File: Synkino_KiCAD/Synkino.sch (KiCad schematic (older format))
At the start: 88 parts

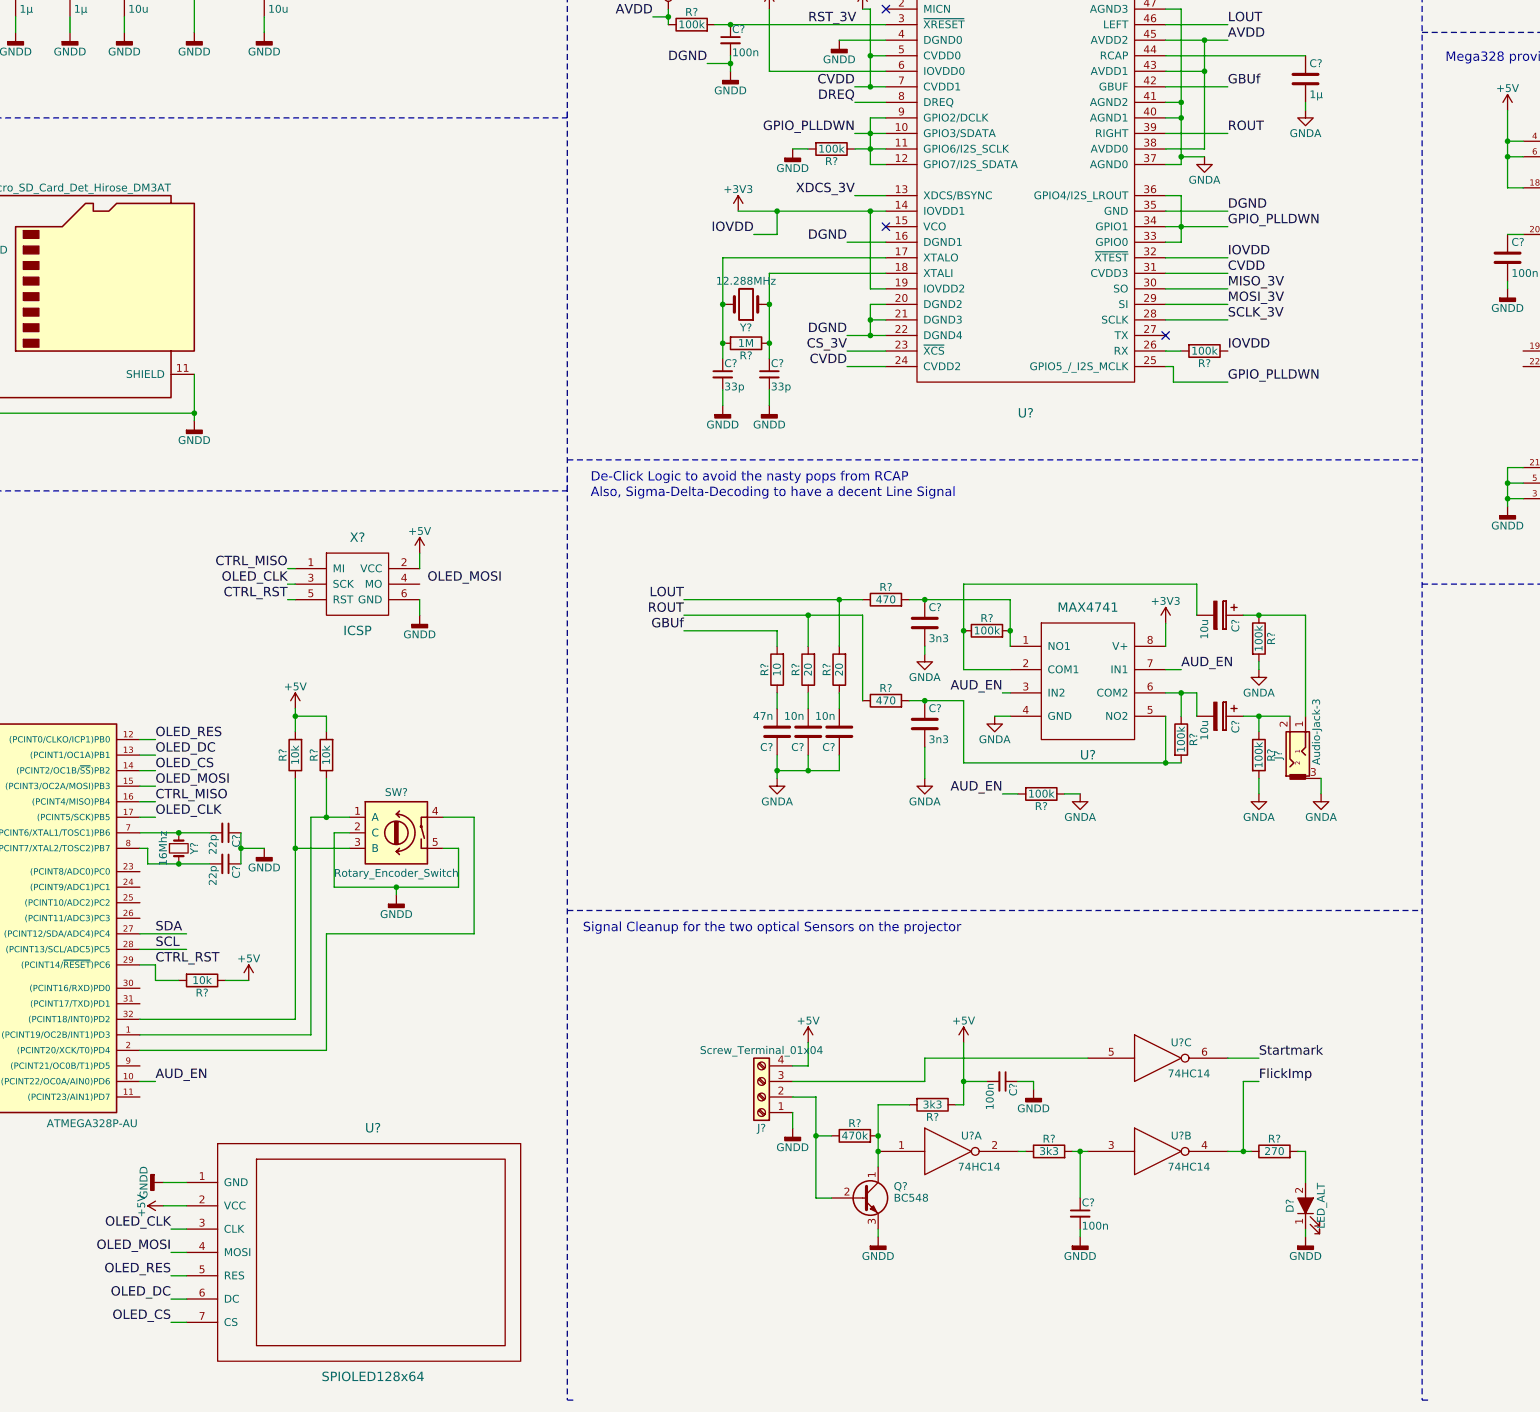
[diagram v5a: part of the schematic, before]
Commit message: Adding ICSP to both uCs
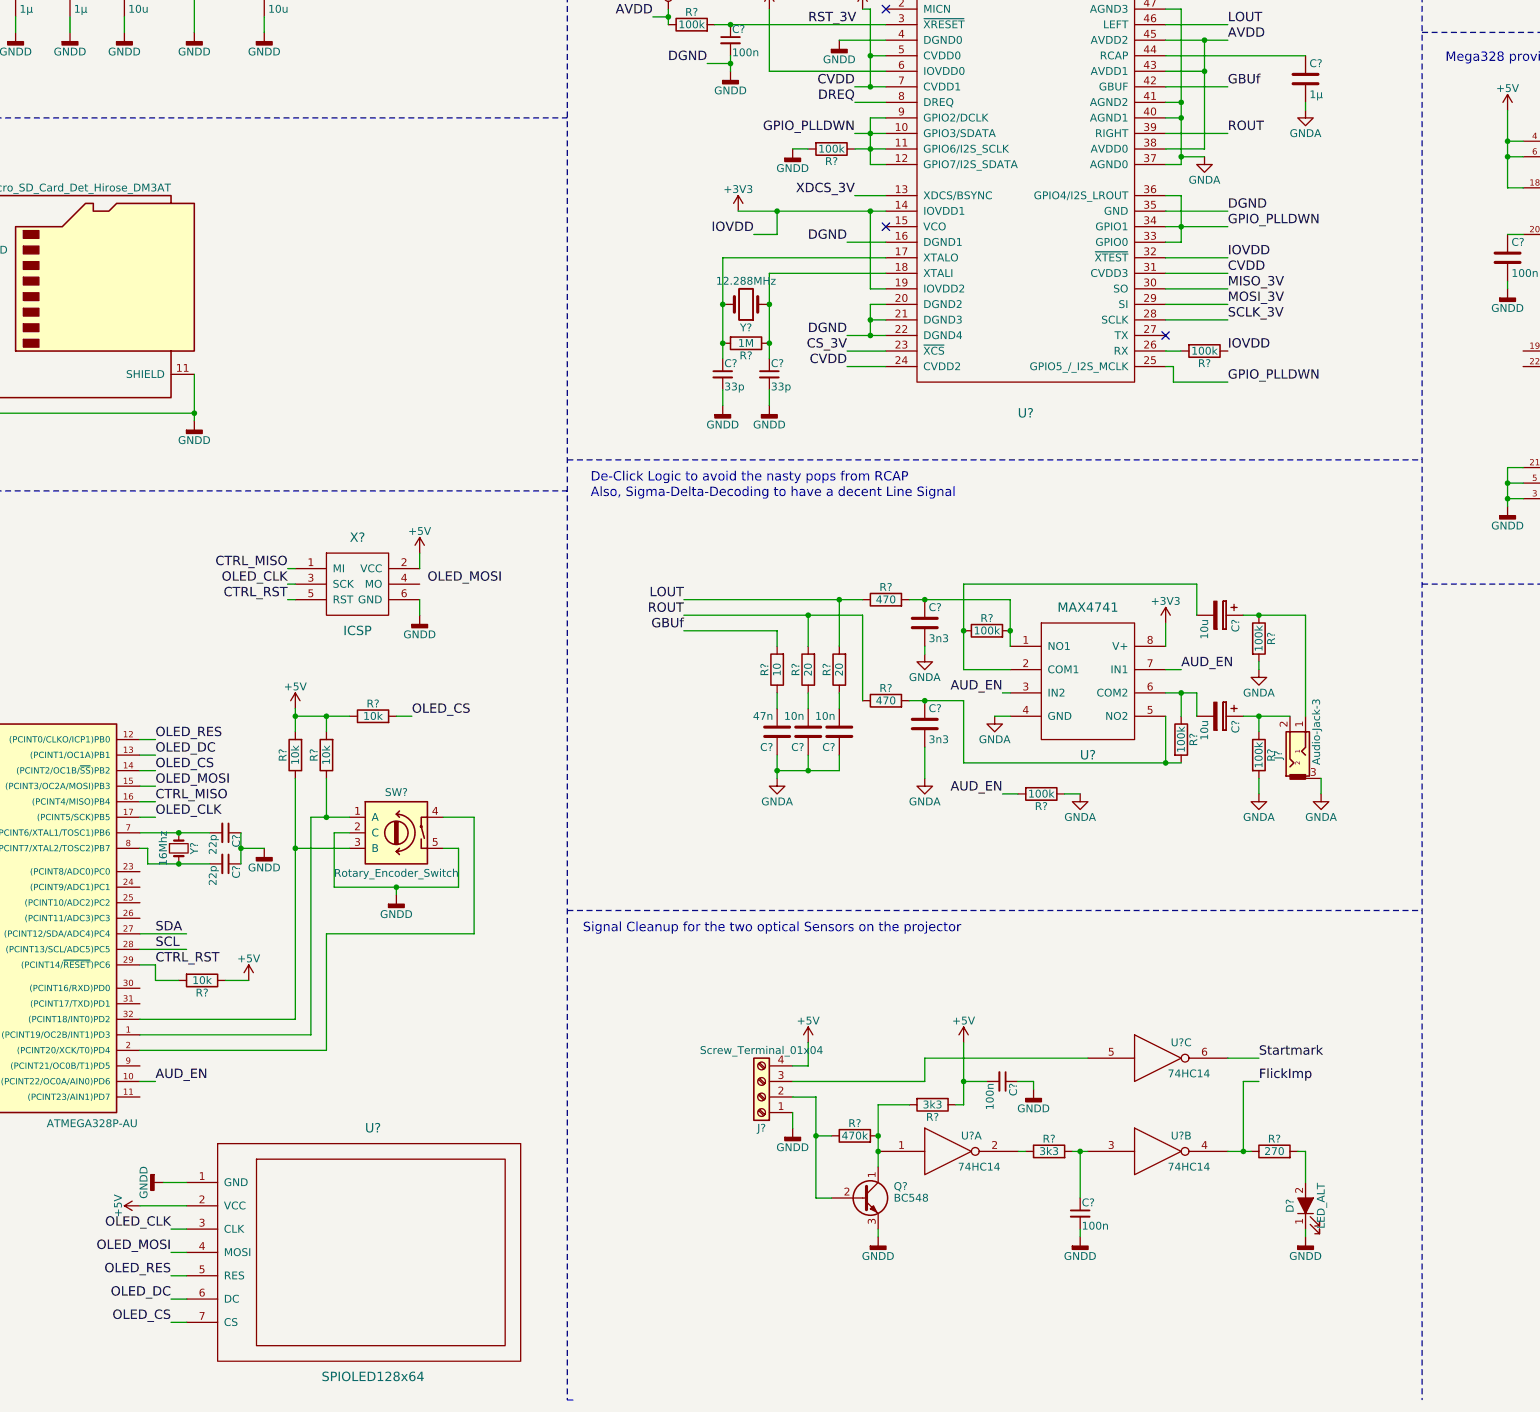
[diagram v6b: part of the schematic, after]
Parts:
- added R?: 10k, symbol R
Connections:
- net +5V: now also R?.1
- net OLED_CS: now also R?.2
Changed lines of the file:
@@
 L +5V #PWR?
 U 1 1 5A9C29C5
-P 3000 9950
-F 0 "#PWR?" H 3000 9800 50  0001 C CNN
-F 1 "+5V" H 3000 10090 50  0000 C CNN
-F 2 "" H 3000 9950 50  0001 C CNN
-F 3 "" H 3000 9950 50  0001 C CNN
-	1    3000 9950
+P 2850 9950
+F 0 "#PWR?" H 2850 9800 50  0001 C CNN
+F 1 "+5V" H 2850 10090 50  0000 C CNN
+F 2 "" H 2850 9950 50  0001 C CNN
+F 3 "" H 2850 9950 50  0001 C CNN
+	1    2850 9950
 	0    -1   -1   0
 $EndComp
@@
 	3000 9800 3150 9800
 Wire Wire Line
-	3000 9950 3150 9950
+	2850 9950 3150 9950
 Text Label 2950 7450 0    60   ~ 0
 OLED_CLK
@@
 	4050 6900 4050 6800
 Wire Wire Line
-	4050 6800 3850 6800
+	3850 6800 4200 6800
 Connection ~ 3850 6800
 Wire Wire Line
@@
 	5000 7450 4800 7450
 Wire Notes Line
-	5600 500  5600 11200
-Wire Notes Line
 	5600 11200 5650 11200
 Wire Notes Line
 	11100 500  11100 11200
 Wire Notes Line
-	11100 11200 11150 11200
-Wire Notes Line
 	500  2950 5600 2950
 Wire Notes Line
-	5600 2950 5600 2900
-Wire Notes Line
 	500  5350 5600 5350
-Wire Notes Line
-	5600 5350 5600 5250
 Wire Notes Line
 	5600 5150 11100 5150
@@
 Wire Wire Line
 	2900 7650 2900 7750
+Wire Notes Line
+	5600 500  5600 11200
+$Comp
+L R R?
+U 1 1 5A9CE1EA
+P 4350 6800
+F 0 "R?" V 4430 6800 50  0000 C CNN
+F 1 "10k" V 4350 6800 50  0000 C CNN
+F 2 "" V 4280 6800 50  0001 C CNN
+F 3 "" H 4350 6800 50  0001 C CNN
+	1    4350 6800
+	0    -1   -1   0
+$EndComp
+Connection ~ 4050 6800
+Text Label 4600 6800 0    60   ~ 0
+OLED_CS
+Wire Wire Line
+	4500 6800 4600 6800
 $EndSCHEMATC

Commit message: Adding FTDI Jumpers
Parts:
- added C? (x2): 100n, symbol C_Small
- added X? (x2): FTDIconn, symbol FTDIconn
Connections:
- net +5V: now also X?.3 (VCC), X?.3 (VCC)
- net CTRL_RST: now also C?.1
- net GNDD: now also X?.1 (GND), X?.1 (GND), X?.2 (CTS), X?.2 (CTS)
- net ~RST: now also C?.1
- net AU_RXD: now reaches U?.30 ((PCINT16/RXD)PD0)
- net AU_RXD: now also X?.4 (TXO)
- net AU_TXD: now reaches U?.31 ((PCINT17/TXD)PD1)
- net AU_TXD: now also X?.5 (RXI)
- net CTRL_RXD: now reaches U?.30 ((PCINT16/RXD)PD0)
- net CTRL_RXD: now also X?.4 (TXO)
- net CTRL_TXD: now reaches U?.31 ((PCINT17/TXD)PD1)
- net CTRL_TXD: now also X?.5 (RXI)
- new net: C?.2, X?.6 (DTR) (x2)
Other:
- moved on the sheet: R?
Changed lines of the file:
@@
 LIBS:spioled128x64
 LIBS:icsp
+LIBS:ftdi
 LIBS:Synkino-cache
 EELAYER 25 0
@@
 $EndComp
 Wire Wire Line
-	11750 5200 11650 5200
+	11550 5200 11750 5200
 Wire Wire Line
 	11650 5200 11650 5450
@@
 Text Label 13750 4450 0    60   ~ 0
 SCL
-Wire Wire Line
-	13650 4350 13950 4350
-Wire Wire Line
-	13650 4450 13950 4450
 $Comp
 L R R?
 U 1 1 5A9D1C9B
+P 14100 4150
+F 0 "R?" V 14180 4150 50  0000 C CNN
+F 1 "10k" V 14100 4150 50  0000 C CNN
+F 2 "" V 14030 4150 50  0001 C CNN
+F 3 "" H 14100 4150 50  0001 C CNN
+	1    14100 4150
+	0    1    1    0
+$EndComp
+$Comp
+L R R?
+U 1 1 5A9D1E44
 P 14100 4350
 F 0 "R?" V 14180 4350 50  0000 C CNN
@@
 	0    1    1    0
 $EndComp
-$Comp
-L R R?
-U 1 1 5A9D1E44
-P 14100 4450
-F 0 "R?" V 14180 4450 50  0000 C CNN
-F 1 "10k" V 14100 4450 50  0000 C CNN
-F 2 "" V 14030 4450 50  0001 C CNN
-F 3 "" H 14100 4450 50  0001 C CNN
-	1    14100 4450
-	0    1    1    0
-$EndComp
-Wire Wire Line
-	14250 4350 14300 4350
-Wire Wire Line
-	14300 4350 14300 4550
+Wire Wire Line
+	14300 4150 14300 4550
 Connection ~ 14300 4550
-Wire Wire Line
-	14250 4450 14300 4450
-Connection ~ 14300 4450
 $Comp
 L ATMEGA328P-AU U?
@@
 L R R?
 U 1 1 5A9D65E3
-P 3250 8500
-F 0 "R?" V 3330 8500 50  0000 C CNN
-F 1 "10k" V 3250 8500 50  0000 C CNN
-F 2 "" V 3180 8500 50  0001 C CNN
-F 3 "" H 3250 8500 50  0001 C CNN
-	1    3250 8500
+P 3600 8400
+F 0 "R?" V 3680 8400 50  0000 C CNN
+F 1 "10k" V 3600 8400 50  0000 C CNN
+F 2 "" V 3530 8400 50  0001 C CNN
+F 3 "" H 3600 8400 50  0001 C CNN
+	1    3600 8400
 	0    1    1    0
 $EndComp
@@
 L +5V #PWR?
 U 1 1 5A9D65E9
-P 3550 8500
-F 0 "#PWR?" H 3550 8350 50  0001 C CNN
-F 1 "+5V" H 3550 8640 50  0000 C CNN
-F 2 "" H 3550 8500 50  0001 C CNN
-F 3 "" H 3550 8500 50  0001 C CNN
-	1    3550 8500
+P 3750 8250
+F 0 "#PWR?" H 3750 8100 50  0001 C CNN
+F 1 "+5V" H 3750 8390 50  0000 C CNN
+F 2 "" H 3750 8250 50  0001 C CNN
+F 3 "" H 3750 8250 50  0001 C CNN
+	1    3750 8250
 	1    0    0    -1
 $EndComp
@@
 CTRL_RST
 Wire Wire Line
-	2850 8400 2950 8400
+	2850 8400 3450 8400
 Text Label 3800 6050 2    60   ~ 0
 CTRL_RST
@@
 Wire Wire Line
 	3800 6050 3850 6050
-Wire Wire Line
-	2950 8400 2950 8500
-Wire Wire Line
-	2950 8500 3100 8500
-Wire Wire Line
-	3400 8500 3550 8500
 Wire Wire Line
 	2850 7650 2900 7650
@@
 Wire Wire Line
 	4500 6800 4600 6800
+$Comp
+L FTDIconn X?
+U 1 1 5A9C7C58
+P 15000 4350
+F 0 "X?" H 15000 4800 60  0000 C CNN
+F 1 "FTDIconn" H 15000 3900 60  0000 C CNN
+F 2 "" H 15000 4400 60  0001 C CNN
+F 3 "" H 15000 4400 60  0001 C CNN
+	1    15000 4350
+	1    0    0    -1
+$EndComp
+Text Label 11550 5200 2    60   ~ 0
+GNDD
+Connection ~ 11650 5200
+Text Label 15400 4100 0    60   ~ 0
+GNDD
+Text Label 15400 4200 0    60   ~ 0
+GNDD
+Text Label 11550 2950 2    60   ~ 0
+5V
+Wire Wire Line
+	11550 2950 11650 2950
+Connection ~ 11650 2950
+Text Label 15400 4300 0    60   ~ 0
+5V
+Wire Wire Line
+	15300 4100 15400 4100
+Wire Wire Line
+	15300 4200 15400 4200
+Wire Wire Line
+	15300 4300 15400 4300
+Text Label 13750 4700 0    60   ~ 0
+AU_RXD
+Text Label 13750 4800 0    60   ~ 0
+AU_TXD
+Wire Wire Line
+	13650 4700 13750 4700
+Wire Wire Line
+	13650 4800 13750 4800
+Text Label 15400 4400 0    60   ~ 0
+AU_RXD
+Text Label 15400 4500 0    60   ~ 0
+AU_TXD
+Wire Wire Line
+	15300 4400 15400 4400
+Wire Wire Line
+	15300 4500 15400 4500
+$Comp
+L C_Small C?
+U 1 1 5A9C9C74
+P 15500 4600
+F 0 "C?" H 15510 4670 50  0000 L CNN
+F 1 "100n" H 15510 4520 50  0000 L CNN
+F 2 "" H 15500 4600 50  0001 C CNN
+F 3 "" H 15500 4600 50  0001 C CNN
+	1    15500 4600
+	0    1    1    0
+$EndComp
+Wire Wire Line
+	15300 4600 15400 4600
+Text Label 15650 4600 0    60   ~ 0
+~RST
+Wire Wire Line
+	15600 4600 15650 4600
+Wire Wire Line
+	13650 4350 13750 4350
+Wire Wire Line
+	13950 4150 13750 4150
+Wire Wire Line
+	13750 4150 13750 4350
+Wire Wire Line
+	13650 4450 13950 4450
+Wire Wire Line
+	13950 4450 13950 4350
+Wire Wire Line
+	14250 4150 14300 4150
+Wire Wire Line
+	14250 4350 14300 4350
+Connection ~ 14300 4350
+$Comp
+L FTDIconn X?
+U 1 1 5A9CBCDC
+P 1600 6150
+F 0 "X?" H 1600 6600 60  0000 C CNN
+F 1 "FTDIconn" H 1600 5700 60  0000 C CNN
+F 2 "" H 1600 6200 60  0001 C CNN
+F 3 "" H 1600 6200 60  0001 C CNN
+	1    1600 6150
+	1    0    0    -1
+$EndComp
+Text Label 2000 5900 0    60   ~ 0
+GNDD
+Text Label 2000 6000 0    60   ~ 0
+GNDD
+Text Label 2000 6100 0    60   ~ 0
+5V
+Wire Wire Line
+	1900 5900 2000 5900
+Wire Wire Line
+	1900 6000 2000 6000
+Wire Wire Line
+	1900 6100 2000 6100
+Text Label 2000 6200 0    60   ~ 0
+CTRL_RXD
+Text Label 2000 6300 0    60   ~ 0
+CTRL_TXD
+Wire Wire Line
+	1900 6200 2000 6200
+Wire Wire Line
+	1900 6300 2000 6300
+$Comp
+L C_Small C?
+U 1 1 5A9CBCEC
+P 2100 6400
+F 0 "C?" H 2110 6470 50  0000 L CNN
+F 1 "100n" H 2110 6320 50  0000 L CNN
+F 2 "" H 2100 6400 50  0001 C CNN
+F 3 "" H 2100 6400 50  0001 C CNN
+	1    2100 6400
+	0    1    1    0
+$EndComp
+Wire Wire Line
+	1900 6400 2000 6400
+Text Label 2250 6400 0    60   ~ 0
+CTRL_RST
+Wire Wire Line
+	2200 6400 2250 6400
+Text Label 2950 8650 0    60   ~ 0
+CTRL_TXD
+Wire Wire Line
+	3750 8400 3750 8250
+Text Label 2950 8550 0    60   ~ 0
+CTRL_RXD
+Wire Wire Line
+	2850 8550 2950 8550
+Wire Wire Line
+	2850 8650 2950 8650
 $EndSCHEMATC

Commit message: Fixing PSU
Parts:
- added J?: Screw_Terminal_01x02, symbol Screw_Terminal_01x02
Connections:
- net +5V: now also C?.1, U?.3 (EN2), U?.4 (EN1), U?.5 (VIN)
- net GNDD: now also J?.1 (Pin_1)
- removed net VDC: C?.1, C?.1, U?.3 (EN2), U?.3 (VI), U?.4 (EN1), U?.5 (VIN)
- new net: C?.1, J?.2 (Pin_2), U?.3 (VI)
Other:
- moved on the sheet: C?, U?
